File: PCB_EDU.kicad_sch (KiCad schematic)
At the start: 0 parts

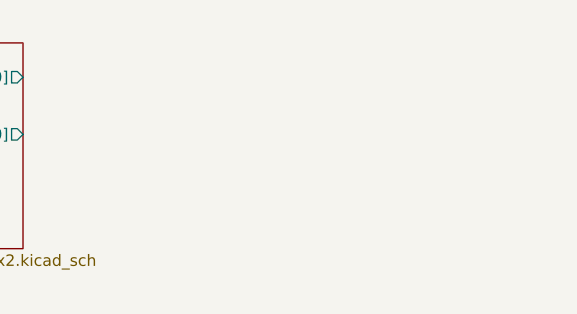
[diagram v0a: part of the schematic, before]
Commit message: feat: add 4-bit register_file
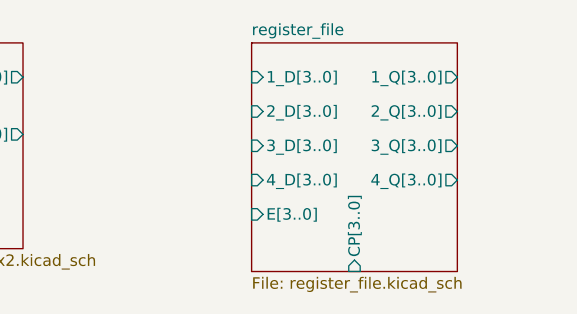
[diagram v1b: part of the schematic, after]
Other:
- added sheet register_file (register_file.kicad_sch)
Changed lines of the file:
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@@
+		)
+	)
+	(sheet
+		(at 101.6 76.2)
+		(size 22.86 25.4)
+		(exclude_from_sim no)
+		(in_bom yes)
+		(on_board yes)
+		(dnp no)
+		(fields_autoplaced yes)
+		(stroke
+			(width 0.1524)
+			(type solid)
+		)
+		(fill
+			(color 0 0 0 0)
+		)
+		(property "Sheetname" "register_file"
+			(at 101.6 75.4884 0)
+			(show_name no)
+			(do_not_autoplace no)
+			(effects
+				(font
+					(size 1.27 1.27)
+				)
+				(justify left bottom)
+			)
+		)
+		(property "Sheetfile" "register_file.kicad_sch"
+			(at 101.6 102.1846 0)
+			(show_name no)
+			(do_not_autoplace no)
+			(effects
+				(font
+					(size 1.27 1.27)
+				)
+				(justify left top)
+			)
+		)
+		(pin "1_D[3..0]" input
+			(at 101.6 80.01 180)
+			(effects
+				(font
+					(size 1.27 1.27)
+				)
+				(justify left)
+			)
+		)
+		(pin "2_D[3..0]" input
+			(at 101.6 83.82 180)
+			(effects
+				(font
+					(size 1.27 1.27)
+				)
+				(justify left)
+			)
+		)
+		(pin "4_D[3..0]" input
+			(at 101.6 91.44 180)
+			(effects
+				(font
+					(size 1.27 1.27)
+				)
+				(justify left)
+			)
+		)
+		(pin "3_D[3..0]" input
+			(at 101.6 87.63 180)
+			(effects
+				(font
+					(size 1.27 1.27)
+				)
+				(justify left)
+			)
+		)
+		(pin "E[3..0]" input
+			(at 101.6 95.25 180)
+			(effects
+				(font
+					(size 1.27 1.27)
+				)
+				(justify left)
+			)
+		)
+		(pin "3_Q[3..0]" output
+			(at 124.46 87.63 0)
+			(effects
+				(font
+					(size 1.27 1.27)
+				)
+				(justify right)
+			)
+		)
+		(pin "2_Q[3..0]" output
+			(at 124.46 83.82 0)
+			(effects
+				(font
+					(size 1.27 1.27)
+				)
+				(justify right)
+			)
+		)
+		(pin "4_Q[3..0]" output
+			(at 124.46 91.44 0)
+			(effects
+				(font
+					(size 1.27 1.27)
+				)
+				(justify right)
+			)
+		)
+		(pin "1_Q[3..0]" output
+			(at 124.46 80.01 0)
+			(effects
+				(font
+					(size 1.27 1.27)
+				)
+				(justify right)
+			)
+		)
+		(pin "CP[3..0]" input
+			(at 113.03 101.6 270)
+			(effects
+				(font
+					(size 1.27 1.27)
+				)
+				(justify left)
+			)
+		)
+		(instances
+			(project "PCB_EDU"
+				(path "/2f9d63ef-4408-4e64-a9eb-2669ac711241"
+					(page "2")
+				)
+			)
 		)
 	)

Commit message: feat: add 4-1 mux part
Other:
- added sheet 4-1_mux_x4_1 (4-1_mux_x4.kicad_sch)
- added sheet 4-1_mux_x4_2 (4-1_mux_x4.kicad_sch)
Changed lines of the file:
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@@
 		)
 		(pin "1_S[1..0]" input
-			(at 63.5 99.06 270)
+			(at 58.42 92.71 180)
 			(effects
 				(font
@@
 		)
 		(pin "2_S[1..0]" input
-			(at 71.12 99.06 270)
+			(at 58.42 96.52 180)
 			(effects
 				(font
@@
 				(path "/2f9d63ef-4408-4e64-a9eb-2669ac711241"
 					(page "7")
+				)
+			)
+		)
+	)
+	(sheet
+		(at 154.94 76.2)
+		(size 19.05 24.13)
+		(exclude_from_sim no)
+		(in_bom yes)
+		(on_board yes)
+		(dnp no)
+		(fields_autoplaced yes)
+		(stroke
+			(width 0.1524)
+			(type solid)
+		)
+		(fill
+			(color 0 0 0 0)
+		)
+		(property "Sheetname" "4-1_mux_x4_1"
+			(at 154.94 75.4884 0)
+			(show_name no)
+			(do_not_autoplace no)
+			(effects
+				(font
+					(size 1.27 1.27)
+				)
+				(justify left bottom)
+			)
+		)
+		(property "Sheetfile" "4-1_mux_x4.kicad_sch"
+			(at 154.94 100.9146 0)
+			(show_name no)
+			(do_not_autoplace no)
+			(effects
+				(font
+					(size 1.27 1.27)
+				)
+				(justify left top)
+			)
+		)
+		(pin "Y[3..0]" output
+			(at 173.99 85.09 0)
+			(effects
+				(font
+					(size 1.27 1.27)
+				)
+				(justify right)
+			)
+		)
+		(pin "1_X[3..0]" input
+			(at 154.94 78.74 180)
+			(effects
+				(font
+					(size 1.27 1.27)
+				)
+				(justify left)
+			)
+		)
+		(pin "2_X[3..0]" input
+			(at 154.94 82.55 180)
+			(effects
+				(font
+					(size 1.27 1.27)
+				)
+				(justify left)
+			)
+		)
+		(pin "3_X[3..0]" input
+			(at 154.94 86.36 180)
+			(effects
+				(font
+					(size 1.27 1.27)
+				)
+				(justify left)
+			)
+		)
+		(pin "4_X[3..0]" input
+			(at 154.94 90.17 180)
+			(effects
+				(font
+					(size 1.27 1.27)
+				)
+				(justify left)
+			)
+		)
+		(pin "S[1..0]" input
+			(at 154.94 96.52 180)
+			(effects
+				(font
+					(size 1.27 1.27)
+				)
+				(justify left)
+			)
+		)
+		(instances
+			(project "PCB_EDU"
+				(path "/2f9d63ef-4408-4e64-a9eb-2669ac711241"
+					(page "3")
+				)
+			)
+		)
+	)
+	(sheet
+		(at 154.94 113.03)
+		(size 19.05 24.13)
+		(exclude_from_sim no)
+		(in_bom yes)
+		(on_board yes)
+		(dnp no)
+		(fields_autoplaced yes)
+		(stroke
+			(width 0.1524)
+			(type solid)
+		)
+		(fill
+			(color 0 0 0 0)
+		)
+		(property "Sheetname" "4-1_mux_x4_2"
+			(at 154.94 112.3184 0)
+			(show_name no)
+			(do_not_autoplace no)
+			(effects
+				(font
+					(size 1.27 1.27)
+				)
+				(justify left bottom)
+			)
+		)
+		(property "Sheetfile" "4-1_mux_x4.kicad_sch"
+			(at 154.94 137.7446 0)
+			(show_name no)
+			(do_not_autoplace no)
+			(effects
+				(font
+					(size 1.27 1.27)
+				)
+				(justify left top)
+			)
+		)
+		(pin "Y[3..0]" output
+			(at 173.99 121.92 0)
+			(effects
+				(font
+					(size 1.27 1.27)
+				)
+				(justify right)
+			)
+		)
+		(pin "1_X[3..0]" input
+			(at 154.94 115.57 180)
+			(effects
+				(font
+					(size 1.27 1.27)
+				)
+				(justify left)
+			)
+		)
+		(pin "2_X[3..0]" input
+			(at 154.94 119.38 180)
+			(effects
+				(font
+					(size 1.27 1.27)
+				)
+				(justify left)
+			)
+		)
+		(pin "3_X[3..0]" input
+			(at 154.94 123.19 180)
+			(effects
+				(font
+					(size 1.27 1.27)
+				)
+				(justify left)
+			)
+		)
+		(pin "4_X[3..0]" input
+			(at 154.94 127 180)
+			(effects
+				(font
+					(size 1.27 1.27)
+				)
+				(justify left)
+			)
+		)
+		(pin "S[1..0]" input
+			(at 154.94 133.35 180)
+			(effects
+				(font
+					(size 1.27 1.27)
+				)
+				(justify left)
+			)
+		)
+		(instances
+			(project "PCB_EDU"
+				(path "/2f9d63ef-4408-4e64-a9eb-2669ac711241"
+					(page "4")
 				)
 			)
@@
 		)
 		(pin "CP[3..0]" input
-			(at 113.03 101.6 270)
-			(effects
-				(font
+			(at 101.6 99.06 180)
+			(effects
+				(font

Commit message: feat: add 1-2 demux part
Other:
- added sheet 1-2_demux_x4_1 (1-2_demux_x4_1.kicad_sch)
- added sheet 1-2_demux_x4_2 (1-2_demux_x4_1.kicad_sch)

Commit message: feat: pcb schematic finalization
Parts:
- added C19, C2, C20: 100n, Capacitor_SMD:C_0603_1608Metric_Pad1.08x0.95mm_HandSolder, symbol Device:C
- added C3: 10u, Capacitor_SMD:C_0805_2012Metric_Pad1.18x1.45mm_HandSolder, symbol Device:C
- added D1, D2, D23, D24, D25, D26, D27, D28, D29, D3, D30, D31, D32, D33, D4, D5: LED, LED_THT:LED_D5.0mm, symbol Device:LED
- added D22: SMAJ5.0A, Diode_SMD:D_SMA, symbol Diode:SMAJ5.0A
- added F1: PPTC, Fuse:Fuse_1812_4532Metric_Pad1.30x3.40mm_HandSolder, symbol Device:Polyfuse
- added J1: USB_C_16_PIN, Connector_USB:USB_C_Receptacle_G-Switch_GT-USB-7010ASV, symbol Connector:USB_C_Receptacle_USB2.0_16P
- added R1, R2, R26, R27, R28, R29, R3, R30, R31, R32, R33, R34, R35, R36, R4, R5: 1k, Resistor_SMD:R_0603_1608Metric_Pad0.98x0.95mm_HandSolder, symbol Device:R
- added R24, R25: 5.1k, Resistor_SMD:R_0603_1608Metric_Pad0.98x0.95mm_HandSolder, symbol Device:R
- added R6, R7: 10k, Resistor_SMD:R_0603_1608Metric_Pad0.98x0.95mm_HandSolder, symbol Device:R
- added SW1, SW14, SW15, SW16, SW17, SW18, SW19, SW20, SW21, SW22, SW23, SW24: SW_SPDT, pcb_edu:SPDT_switch, symbol Switch:SW_SPDT
- added SW2, SW3: SW_Push, Button_Switch_SMD:SW_Push_1P1T_NO_E-Switch_TL3301NxxxxxG, symbol Switch:SW_Push
- added U10: 74LS32, Package_SO:SOIC-14_3.9x8.7mm_P1.27mm, symbol 74xx:74LS32
- added U11: 74LS283, Package_SO:SOIC-16_3.9x9.9mm_P1.27mm, symbol 74xx:74LS283
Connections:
- new net: D27.1 (K), R30.1
- new net: D4.1 (K), R4.1
- new net: D23.1 (K), R26.1
- new net: D30.1 (K), R33.1
- new net: D24.1 (K), R27.1
- new net: D25.1 (K), R28.1
- new net: D26.1 (K), R29.1
- new net: D2.1 (K), R2.1
- new net: D33.1 (K), R36.1
- new net: D1.1 (K), R1.1
- new net: D31.1 (K), R34.1
- new net: D29.1 (K), R32.1
- new net: D5.1 (K), R5.1
- new net: D28.1 (K), R31.1
- new net: D32.1 (K), R35.1
- new net: J1.A5 (CC1), R25.1
- new net: J1.B5 (CC2), R24.1
- new net: D3.1 (K), R3.1
- new net 1_Y0: U11.5 (A1)
- new net 1_Y1: U10.1
- new net 2_Y0: U11.3 (A2)
- new net 2_Y1: U10.4
- new net 3_Y0: U11.14 (A3)
- new net 3_Y1: U10.9
- new net 4_Y0: U11.12 (A4)
- new net 4_Y1: U10.12
- new net 5_Y0: U11.6 (B1)
- new net 5_Y1: U10.2
- new net 6_Y0: U11.2 (B2)
- new net 6_Y1: U10.5
- new net 7_Y0: U11.15 (B3)
- new net 7_Y1: U10.10
- new net 8_Y0: U11.11 (B4)
- new net 8_Y1: U10.13
- new net ADD0: U11.4 (S1)
- new net ADD1: U11.1 (S2)
- new net ADD2: U11.13 (S3)
- new net ADD3: U11.10 (S4)
- new net C_OUT: SW1.1 (A), U11.9 (C4)
- new net D0: D23.2 (A), SW14.2 (B)
- new net D1: D24.2 (A), SW15.2 (B)
- new net D2: D25.2 (A), SW16.2 (B)
- new net D3: D26.2 (A), SW17.2 (B)
- new net GND: C19.2, C2.2, C20.2, C3.2, D22.2 (A2), J1.A1 (GND), J1.A12 (GND), J1.B1 (GND), J1.B12 (GND), J1.SH (SHIELD), R1.2, R2.2, R24.2, R25.2, R26.2, R27.2, R28.2, R29.2, R3.2, R30.2, R31.2, R32.2, R33.2, R34.2, R35.2, R36.2, R4.2, R5.2, R6.2, R7.2, SW14.1 (A), SW15.1 (A), SW16.1 (A), SW17.1 (A), SW18.1 (A), SW19.1 (A), SW20.1 (A), SW21.1 (A), SW22.1 (A), SW23.1 (A), SW24.1 (A), U10.7 (GND), U11.7 (C0), U11.8 (GND)
- new net LED_OP0: D1.2 (A)
- new net LED_OP1: D2.2 (A)
- new net LED_OP2: D3.2 (A)
- new net LED_OP3: D4.2 (A), SW1.3 (C)
- new net LED_OP4: D5.2 (A), SW1.2 (B)
- new net OP: D33.2 (A), SW24.2 (B)
- new net OR0: U10.3
- new net OR1: U10.6
- new net OR2: U10.8
- new net OR3: U10.11
- new net R00: D29.2 (A), SW20.2 (B)
- new net R01: D30.2 (A), SW21.2 (B)
- new net R10: D31.2 (A), SW22.2 (B)
- new net R11: D32.2 (A), SW23.2 (B)
- new net RSET0: D27.2 (A), SW18.2 (B)
- new net RSET1: D28.2 (A), SW19.2 (B)
- new net RST: R7.1, SW3.1
- new net VBUS: F1.1, J1.A4 (VBUS), J1.A9 (VBUS), J1.B4 (VBUS), J1.B9 (VBUS)
- new net VDD: C19.1, C2.1, C20.1, C3.1, D22.1 (A1), F1.2, SW14.3 (C), SW15.3 (C), SW16.3 (C), SW17.3 (C), SW18.3 (C), SW19.3 (C), SW2.2, SW20.3 (C), SW21.3 (C), SW22.3 (C), SW23.3 (C), SW24.3 (C), SW3.2, U10.14 (VCC), U11.16 (VCC)
- new net WE: R6.1, SW2.1
- no-connect marks 0 -> 6
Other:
- added sheet 2-1_mux_x4 (2-1_mux_x4.kicad_sch)
- added sheet led_matrix (led_matrix.kicad_sch)
- sheet 1-2_demux_x4_1 ports: added S0, X[3..0]; removed 1_S0, 1_X, 2_S0, 2_X, 3_S0, 3_X, 4_S0, 4_X
- sheet 1-2_demux_x4_2 ports: added S0, X[3..0]; removed 1_S0, 1_X, 2_S0, 2_X, 3_S0, 3_X, 4_S0, 4_X
- sheet register_file ports: added RST; removed none

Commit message: feat: pcb board finalization
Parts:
- added D34: LED, LED_SMD:LED_0805_2012Metric_Pad1.15x1.40mm_HandSolder, symbol Device:LED
- added H1, H2, H3, H4: MH_P, MountingHole:MountingHole_5.3mm_M5_DIN965_Pad, symbol Mechanical:MountingHole_Pad
- added R37: 1k, Resistor_SMD:R_0603_1608Metric_Pad0.98x0.95mm_HandSolder, symbol Device:R
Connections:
- net GND: now also H1.1, H2.1, H3.1, H4.1, R37.2
- net VDD: now also D34.2 (A)
- new net: D34.1 (K), R37.1
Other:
- moved on the sheet: D23, D24, D25, D26, D27, D28, D29, D30, D31, D32, R26, R27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
